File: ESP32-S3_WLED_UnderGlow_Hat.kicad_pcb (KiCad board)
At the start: 6 copper layers, 31 x 29.2 mm, 142 parts, among them CN301 SM32B-NSHDZS-1-TF, CN302 SM32B-NSHDZS-1-TF, Q901 NTLJS17D0P03P8Z, U701 TCAN4550-Q1, U702 74LV1T125, U801 74LV1T125, U802 74LV1T125, U803 74LV1T125, U804 74LV1T125, U805 74LV1T125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

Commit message: Update .gitignore, ESP32-S3_WLED_UnderGlow_Hat-2026-05-05_083139.zip, ESP32-S3_WLED_UnderGlow_Hat.kicad_pcb, and 1 more file
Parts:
- added C717: 0.1uF, My Capacitors:C_0201_Dense, F.Cu at (192.0, 106.1)
- added C821: 0.1uF, My Capacitors:C_0201_Dense, F.Cu at (199.6, 107.7)
- added C822: 0.1uF, My Capacitors:C_0201_Dense, F.Cu at (199.6, 109.2)
- added R809: 33R, My Resistors:R_0201_Dense, F.Cu at (201.5, 104.6)
- added R810: 33R, My Resistors:R_0201_Dense, F.Cu at (201.5, 106.1)
- added R811: 5k1, My Resistors:R_0201_Dense, F.Cu at (201.5, 107.7)
- added R812: 33R, My Resistors:R_0201_Dense, F.Cu at (201.5, 109.2)
- added R813: 0R, My Resistors:R_0201_Dense, F.Cu at (201.5, 110.8)
- C813, C815, C817, R704, U702, Y701: moved to F.Cu
- C814: value 22uF -> 1uF; footprint My Capacitors:C_0603_Dense -> My Capacitors:C_0201_Dense
- C818: value 4.7nF -> 1uF; moved to F.Cu
- C819: value 1uF -> 0.1uF; moved to F.Cu
- C820: value 4.7nF -> 0.1uF; moved to F.Cu
- D815, D816: value D15V0H1U2LP-7B -> SZESD7241N2T5G; moved to F.Cu
- R807, R808: value 470R -> 33R; moved to F.Cu
- U806: value PCM1808 -> ES7241D; footprint My Package_SO:TSSOP-14_4.4x5mm_P0.65mm -> Package_DFN_QFN:QFN-16-1EP_3x3mm_P0.5mm_EP1.7x1.7mm
- moved D816 41.2 mm to (207.3, 111.9), turned to 0 degrees
- moved D815 40.8 mm to (207.3, 110.0), turned to 0 degrees
- moved C916 36.3 mm to (197.7, 118.0), turned to 0 degrees
- moved C819 36.2 mm to (199.6, 104.6), turned to 0 degrees
- moved C820 35.6 mm to (199.6, 106.1), turned to 0 degrees
- moved C816 33.7 mm to (204.2, 112.5), turned to 0 degrees
- moved R808 33.1 mm to (199.6, 112.3), turned to 0 degrees
- moved R807 32.6 mm to (199.6, 110.8), turned to 0 degrees
- moved U806 31.2 mm to (205.5, 106.4), turned to 0 degrees
- moved C817 31.0 mm to (197.7, 110.8), turned to 0 degrees
- moved C707 30.6 mm to (189.3, 109.5), turned to 0 degrees
- moved C814 30.2 mm to (197.7, 107.7), turned to 0 degrees
- moved C818 29.8 mm to (197.7, 112.3), turned to 0 degrees
- moved C708 28.6 mm to (189.3, 111.8), turned to 0 degrees
- moved C706 27.7 mm to (189.3, 107.2), turned to 0 degrees
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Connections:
- net /IO_Board/CAN Bus/FLTR renamed Net-(U701-FLTR)
- net /IO_Board/CAN Bus/OSC1 renamed Net-(U701-OSC1)
- net /IO_Board/CAN Bus/RST renamed Net-(U701-RST)
- net /IO_Board/FSPIHD renamed /IO_Board/FSPI_{HD}
- net /IO_Board/FSPIWP renamed /IO_Board/FSPI_{WP}
- net /IO_Board/GR86 Inputs/~{Dome_S} renamed Net-(D813-A)
- net /IO_Board/MISO renamed /IO_Board/FSPI_{MISO}
- net /IO_Board/MOSI renamed /IO_Board/FSPI_{MOSI}
- net /IO_Board/SCLK renamed /IO_Board/FSPI_{CLK}
- net /IO_Board/WLED Outputs/SDO_{HSS} renamed /IO_Board/WLED Outputs/SDO
- net /IO_Board/~{FSPICS} renamed /IO_Board/~{FSPI_{CS0}}
- C706 pad 1: +V_{SUP} -> /IO_Board/CAN Bus/V_{CC_{OUT}}
- C710 pad 1: /IO_Board/CAN Bus/V_{CC_{OUT}} -> +V_{SUP}
- C811 pad 1: /IO_Board/GR86 Inputs/V_{REF} -> +3V3
- C811 pad 2: GND -> GNDA
- C812 pad 1: /IO_Board/GR86 Inputs/V_{REF} -> +3V3
- C812 pad 2: GND -> GNDA
- C813 pad 2: GND -> GNDA
- C814 pad 2: GND -> GNDA
- C815 pad 1: +5V_{FUSED} -> +3V3
- C815 pad 2: GND -> GNDA
- C816 pad 1: +5V_{FUSED} -> +3V3
- C816 pad 2: GND -> GNDA
- C817 pad 1: /IO_Board/AUX_{R} -> /IO_Board/GR86 Inputs/RC_{808-817}
- C817 pad 2: Net-(C817-Pad2) -> /IO_Board/GR86 Inputs/A_{IN}L
- C818 pad 1: /IO_Board/GR86 Inputs/V_{IN}R -> /IO_Board/GR86 Inputs/RC_{809-818}
- C818 pad 2: GND -> /IO_Board/GR86 Inputs/A_{IN}R
- C819 pad 1: /IO_Board/AUX_{L} -> /IO_Board/GR86 Inputs/REF_{P}
- C819 pad 2: Net-(C819-Pad2) -> GNDA
- C820 pad 1: /IO_Board/GR86 Inputs/V_{IN}L -> /IO_Board/GR86 Inputs/REF_{P}
- C820 pad 2: GND -> GNDA
- D815 pad 1: /IO_Board/AUX_{R} -> /IO_Board/AUX_{L}
- D816 pad 1: /IO_Board/AUX_{L} -> /IO_Board/AUX_{R}
- H301 pad 11: /IO_Board/Reset Node -> /IO_Board/~{Reset Node}
- H302 pad 15: /IO_Board/MCLK -> /IO_Board/I^{2}S_{MCLK}
- H302 pad 16: /IO_Board/SCK -> /IO_Board/I^{2}S_{SCK}
- H302 pad 17: /IO_Board/SD -> /IO_Board/I^{2}S_{SD}
- H302 pad 6: /IO_Board/WS -> /IO_Board/I^{2}S_{WS}
- R703 pad 1: /IO_Board/Reset Node -> /IO_Board/~{Reset Node}
- R807 pad 1: Net-(C817-Pad2) -> /IO_Board/GR86 Inputs/RR_{807-808}
- R807 pad 2: /IO_Board/GR86 Inputs/V_{IN}R -> /IO_Board/AUX_{L}
- R808 pad 1: Net-(C819-Pad2) -> /IO_Board/GR86 Inputs/RC_{808-817}
- R808 pad 2: /IO_Board/GR86 Inputs/V_{IN}L -> /IO_Board/GR86 Inputs/RR_{807-808}
- R901 pad 1: /IO_Board/WLED Outputs/VDD_{HSS} -> +3V3
- R901 pad 2: +3V3 -> /IO_Board/WLED Outputs/VDD_{HSS}
- U702 pad 1: /IO_Board/Reset Node -> /IO_Board/~{Reset Node}
- U806 pad 1: /IO_Board/GR86 Inputs/V_{REF} -> +3V3
- U806 pad 10: GND -> /IO_Board/GR86 Inputs/A_{IN}R
- U806 pad 11: GND -> +3V3
- U806 pad 12: GND -> GNDA
- U806 pad 13: /IO_Board/GR86 Inputs/V_{IN}L -> /IO_Board/GR86 Inputs/REF_{P}
- U806 pad 14: /IO_Board/GR86 Inputs/V_{IN}R -> +3V3
- U806 pad 2: GND -> /IO_Board/GR86 Inputs/SD_{OUT}
- U806 pad 3: +5V_{FUSED} -> GNDA
- U806 pad 5: GND -> /IO_Board/I^{2}S_{SCK}
- U806 pad 6: /IO_Board/MCLK -> /IO_Board/I^{2}S_{WS}
- U806 pad 7: /IO_Board/WS -> /IO_Board/~{Reset Node}
- U806 pad 8: /IO_Board/SCK -> /IO_Board/GR86 Inputs/A_{IN}L
- U806 pad 9: /IO_Board/SD -> /IO_Board/GR86 Inputs/REF_{Q}
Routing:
- net /IO_Board/~{Reset Node}: track 0.00 -> 30.7 mm, vias 0 -> 2
- net /IO_Board/Reset Node: track 30.7 -> 0.00 mm, vias 2 -> 0
- net (no net): track 0.00 -> 24.1 mm, vias 0 -> 4
- net /IO_Board/GR86 Inputs/V_{IN}L: track 10.9 -> 0.00 mm, vias 2 -> 0
- net /IO_Board/GR86 Inputs/V_{IN}R: track 10.8 -> 0.00 mm, vias 2 -> 0
- net /IO_Board/SCK: track 10.4 -> 0.00 mm
- net /IO_Board/I^{2}S_{SCK}: track 0.00 -> 10.4 mm
- net /IO_Board/MCLK: track 9.81 -> 0.00 mm
- net /IO_Board/I^{2}S_{MCLK}: track 0.00 -> 9.81 mm
- net /IO_Board/SD: track 9.59 -> 0.00 mm
- net /IO_Board/I^{2}S_{SD}: track 0.00 -> 9.59 mm
- net /IO_Board/WS: track 7.62 -> 0.00 mm
- net /IO_Board/I^{2}S_{WS}: track 0.00 -> 7.62 mm
- net /IO_Board/GR86 Inputs/V_{REF}: track 2.32 -> 0.00 mm
- net /IO_Board/WLED Outputs/VDD_{HSS}: vias 1 -> 2
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
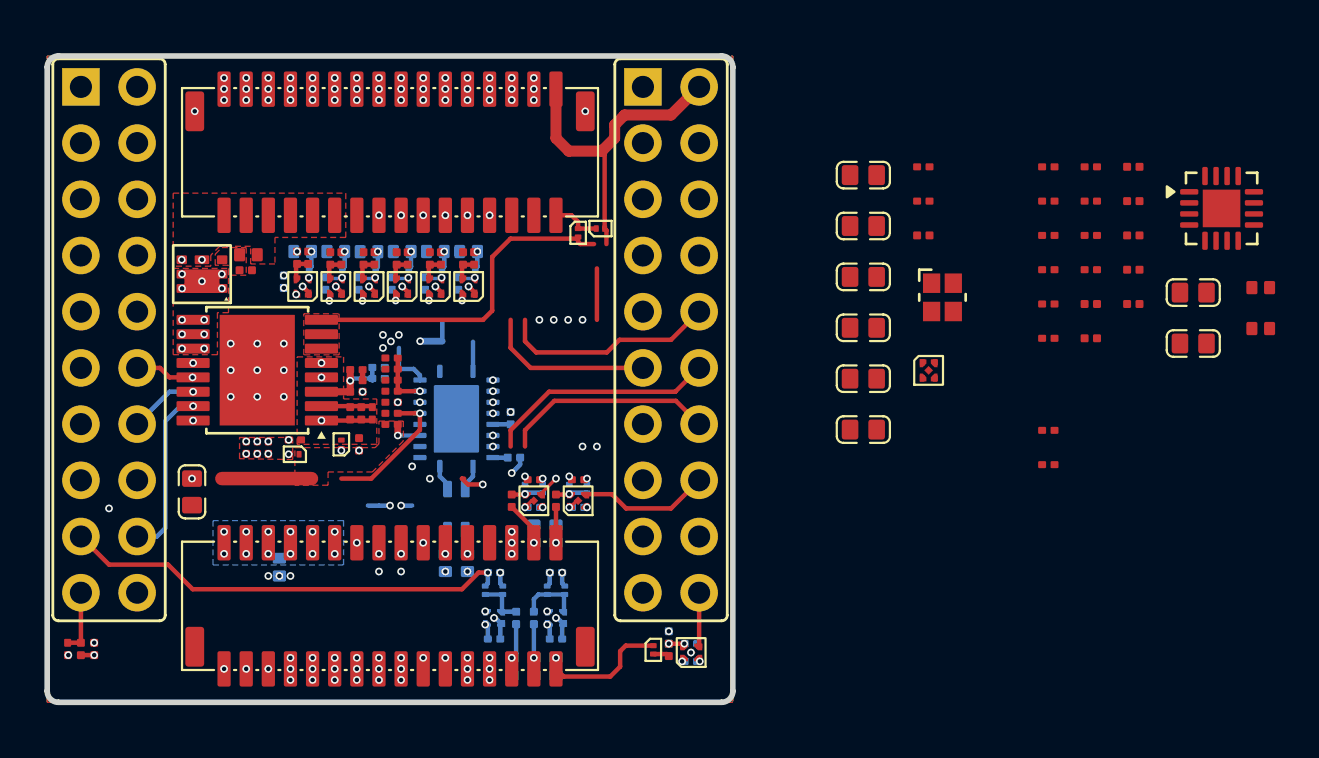
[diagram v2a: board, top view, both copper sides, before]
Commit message: schematic updated with new ESP32-S3_D1_Pico symbol
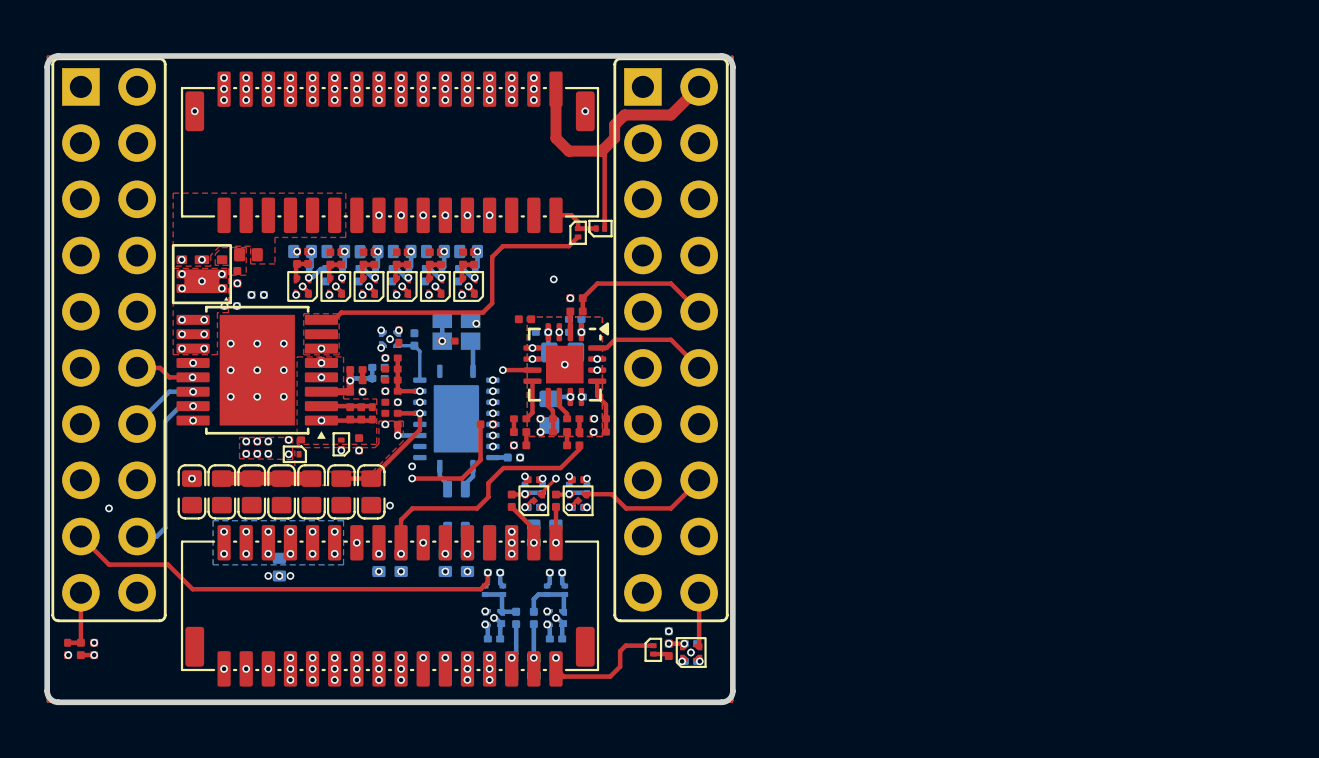
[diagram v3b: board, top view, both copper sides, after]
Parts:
- C811, C812, C813, C814, C815, C816, C906, C916, D815, D816, R704, U702, Y701: moved to B.Cu
- R702: moved to F.Cu
- moved D815 41.7 mm to (167.4, 122.5), turned to -90 degrees
- moved D816 40.3 mm to (168.4, 122.5), turned to -90 degrees
- moved C916 37.6 mm to (160.7, 110.8)
- moved C906 33.0 mm to (164.8, 113.1), turned to -90 degrees
- moved C707 30.6 mm to (160.3, 119.3), turned to -90 degrees
- moved U806 30.5 mm to (175.8, 113.5), turned to -90 degrees
- moved C816 29.3 mm to (175.1, 115.7), turned to -90 degrees
- moved C811 28.6 mm to (175.7, 113.0)
- moved C708 28.6 mm to (161.7, 119.3), turned to -90 degrees
- moved R809 28.0 mm to (176.2, 116.5), turned to 180 degrees
- moved R810 27.6 mm to (176.2, 117.2)
- moved C704 27.6 mm to (165.7, 119.3), turned to -90 degrees
- moved R813 27.5 mm to (174.0, 111.5), turned to 180 degrees
- moved C709 26.8 mm to (163.0, 119.3), turned to -90 degrees
- moved R807 26.6 mm to (173.8, 117.2), turned to 180 degrees
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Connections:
- net /IO_Board/CAN Bus/SDO_{CAN} renamed /IO_Board/CAN Bus/SDO
- net Net-(U701-FLTR) renamed /IO_Board/CAN Bus/FLTR
- net Net-(U701-OSC1) renamed /IO_Board/CAN Bus/OSC1
- net Net-(U701-RST) renamed /IO_Board/CAN Bus/RST
- C906 pad 2: GND0 -> GND2
- C916 pad 1: +V_{SW} -> /IO_Board/WLED Outputs/V_{OUT2}
- C916 pad 2: GND -> GND2
- H302 pad 15: /IO_Board/I^{2}S_{MCLK} -> /IO_Board/I^{2}S_{SD}
- H302 pad 16: /IO_Board/I^{2}S_{SCK} -> /IO_Board/I^{2}S_{MCLK}
- H302 pad 17: /IO_Board/I^{2}S_{SD} -> /IO_Board/I^{2}S_{WS}
- H302 pad 6: /IO_Board/I^{2}S_{WS} -> /IO_Board/I^{2}S_{SCK}
- R909 pad 1: GND -> GND2
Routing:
- net (no net): track 24.1 -> 0.00 mm, vias 4 -> 1
- net /IO_Board/AUX_{R}: track 0.72 -> 11.0 mm
- net /IO_Board/AUX_{L}: track 0.72 -> 9.44 mm, vias 1 -> 2
- net +5V_{FUSED}: track 74.8 -> 67.5 mm, vias 13 -> 11
- net GND2: track 2.37 -> 8.81 mm, vias 3 -> 5
- net /IO_Board/I^{2}S_{SCK}: track 10.4 -> 5.37 mm, vias 0 -> 1
- net /IO_Board/I^{2}S_{MCLK}: track 9.81 -> 5.29 mm
- net /IO_Board/I^{2}S_{SD}: track 9.59 -> 6.66 mm
- net /IO_Board/GR86 Inputs/REF_{P}: track 0.00 -> 2.46 mm
- net /IO_Board/FSPI_{MISO}: track 23.5 -> 21.1 mm
- net /IO_Board/GR86 Inputs/A_{IN}L: track 0.00 -> 1.81 mm
- net /IO_Board/GR86 Inputs/REF_{Q}: track 0.00 -> 1.67 mm
- net /IO_Board/I^{2}S_{WS}: track 7.62 -> 9.04 mm, vias 0 -> 1
- net +3V3: track 3.17 -> 4.58 mm, vias 15 -> 20
- net /IO_Board/WD: track 19.7 -> 20.9 mm
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- added copper zone on B.Cu, net GNDA
- added copper zone on F.Cu, net GNDA
- added copper zone on In1.Cu, net GNDA
- added copper zone on In4.Cu, net GNDA

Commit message: updated pcb with new ESP32-S3_D1_Pico footprint
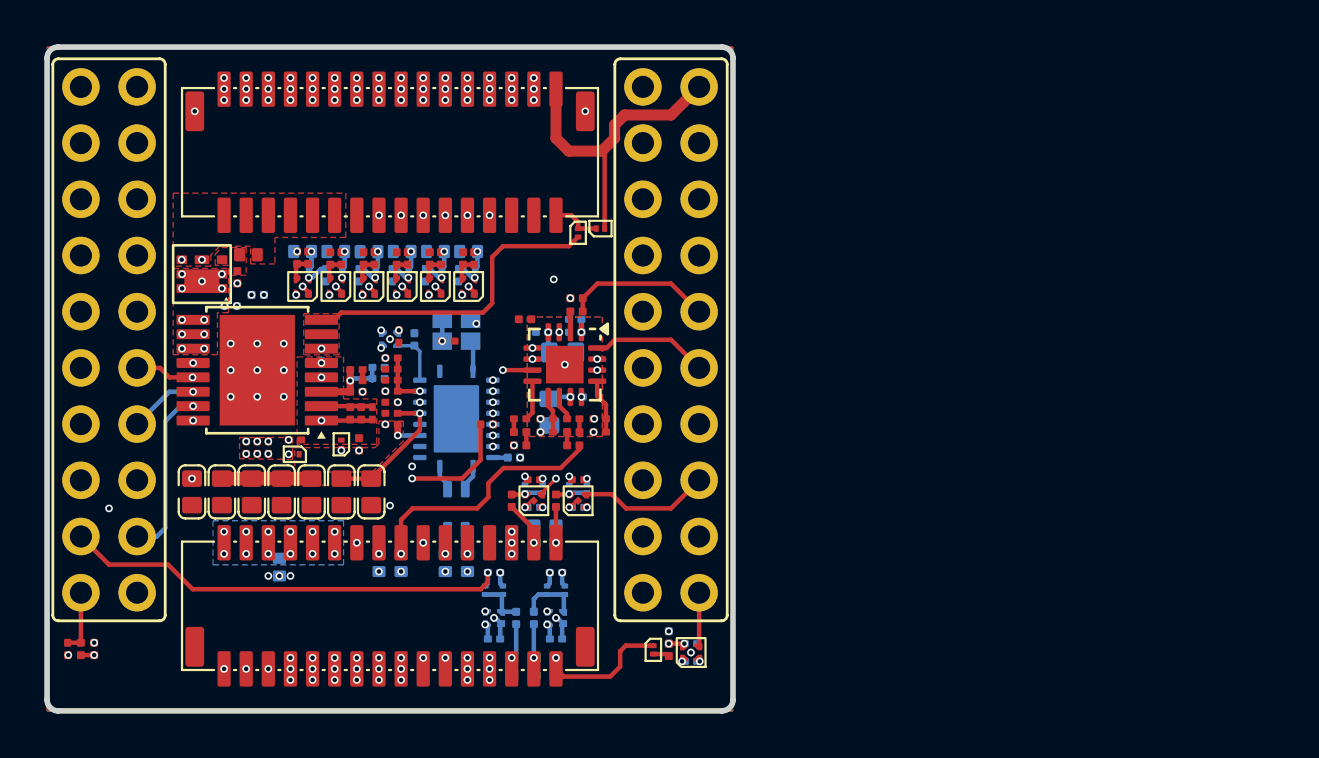
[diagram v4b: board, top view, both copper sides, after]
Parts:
- removed H301, H302: ESP_Header, My Connectors:PinHeader_2x10_P2.54mm_Vertical_THT_BottomMount_TopReference
- added U201: ~, Personal_FootprintLibrary:ESP32-S3_D1_Pico, F.Cu at (167.9, 113.7)
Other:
- board size 31 x 29.2 mm -> 31 x 30 mm
